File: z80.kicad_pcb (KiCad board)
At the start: 2 copper layers, 104.1 x 111.8 mm, 43 parts, among them P1 CONN_02X20, P2 CONN_01X02, SW1 RESET, U1 Z80CPU, U2 74HC04, U3 74LS138, Y1 7.3728MHz

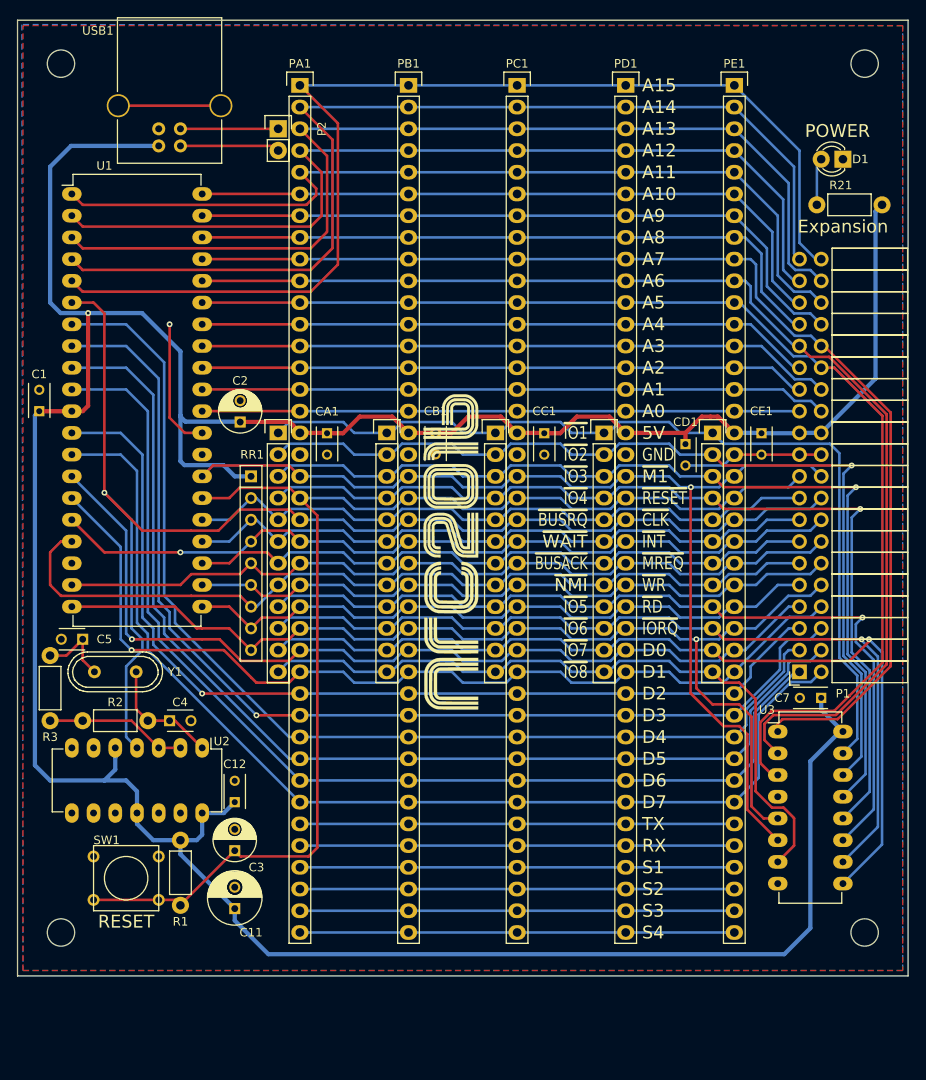
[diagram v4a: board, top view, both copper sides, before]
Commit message: Added new expansion and GAL to layout.
Haven't routed the osc. or the reset.
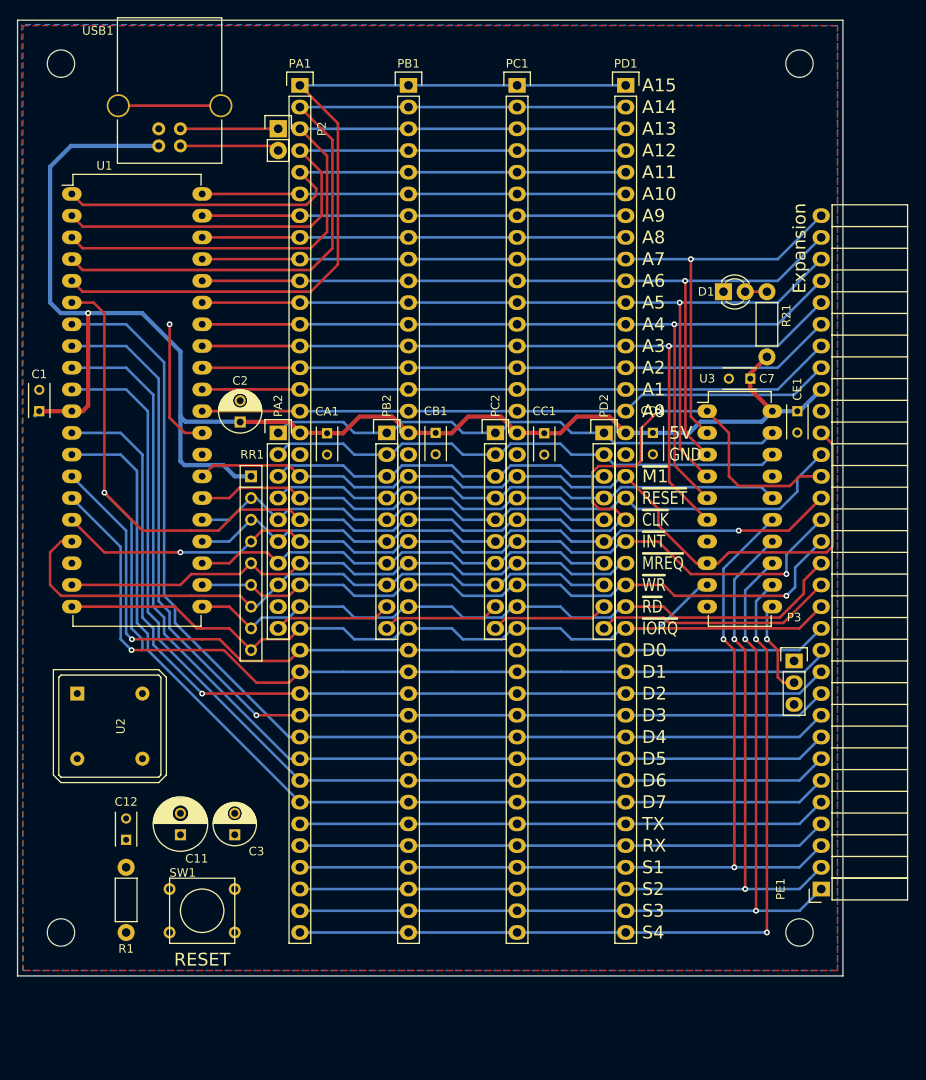
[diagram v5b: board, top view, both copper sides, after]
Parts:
- removed C4, C5: 22pF, Capacitors_ThroughHole:C_Disc_D3_P2.5
- removed G***: LOGO, ncr2016_logo:nrc2016_logo_1200
- removed G***: LOGO, ncr2016_logo:nrc2016_top_logo_1600
- removed P1: CONN_02X20, Socket_Strips:Socket_Strip_Angled_2x20
- removed PE2: CONN_01X12, Socket_Strips:Socket_Strip_Straight_1x12
- removed R2: 1M, Resistors_ThroughHole:Resistor_Horizontal_RM7mm
- removed R3: 1K, Resistors_ThroughHole:Resistor_Horizontal_RM7mm
- removed Y1: 7.3728MHz, Crystals:Crystal_HC49-U_Vertical
- added P3: Jumper, Pin_Headers:Pin_Header_Straight_1x03, F.Cu at (131.4, 105.4)
- PA2, PB2, PC2, PD2: value CONN_01X12 -> CONN_01X10; footprint Socket_Strips:Socket_Strip_Straight_1x12 -> Socket_Strips:Socket_Strip_Straight_1x10
- PE1: value CONN_01X40 -> CONN_01X32; footprint Socket_Strips:Socket_Strip_Straight_1x40 -> Socket_Strips:Socket_Strip_Angled_1x32
- U2: value 74HC04 -> DIP_OSCILLATOR; footprint Housings_DIP:DIP-14_W7.62mm_LongPads -> Oscillators:OSC_DIP8
- U3: value 74LS138 -> ATF16V8CV; footprint Housings_DIP:DIP-16_W7.62mm_LongPads -> Housings_DIP:DIP-20_W7.62mm_LongPads
- moved PE1 94.5 mm to (134.6, 132.1), turned to 90 degrees
- moved U3 38.4 mm to (121.3, 76.2)
- moved C7 38.2 mm to (126.3, 72.4)
- moved R21 22.3 mm to (128.3, 69.8), turned to 90 degrees
- moved D1 20.9 mm to (123.2, 62.2), turned to 0 degrees
- moved C12 13.4 mm to (53.3, 126.3)
- moved U2 11.1 mm to (51.4, 113.0)
- moved C11 10.7 mm to (59.7, 125.7)
- moved SW1 9.67 mm to (62.2, 134.6)
- moved MH2 7.62 mm to (132.1, 35.6)
- moved MH4 7.62 mm to (132.1, 137.2)
- moved R1 7.10 mm to (53.3, 129.5)
- moved CE1 4.92 mm to (131.8, 76.2)
- moved CD1 4.03 mm to (114.9, 78.7)
- moved C3 1.86 mm to (66.0, 125.7)
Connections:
- net /CPU/~BUSACK renamed /~BUSACK
- net /CPU/~BUSRQ renamed /~BUSRQ
- net /CPU/~NMI renamed /~NMI
- C3 pad 1: /CPU/~RESET -> /~RESET
- PA1 pad 1: /CPU/A15 -> /A15
- PA1 pad 10: /CPU/A6 -> /A6
- PA1 pad 11: /CPU/A5 -> /A5
- PA1 pad 12: /CPU/A4 -> /A4
- PA1 pad 13: /CPU/A3 -> /A3
- PA1 pad 14: /CPU/A2 -> /A2
- PA1 pad 15: /CPU/A1 -> /A1
- PA1 pad 16: /CPU/A0 -> /A0
- PA1 pad 19: /CPU/~M1 -> /~M1
- PA1 pad 2: /CPU/A14 -> /A14
- PA1 pad 20: /CPU/~RESET -> /~RESET
- PA1 pad 21: /CPU/~CLK -> /~CLK
- PA1 pad 22: /CPU/~INT -> /~INT
- PA1 pad 23: /CPU/~MREQ -> /~MREQ
- PA1 pad 24: /CPU/~WR -> /~WR
- PA1 pad 25: /CPU/~RD -> /~RD
- PA1 pad 26: /CPU/~IORQ -> /~IORQ
- PA1 pad 27: /CPU/D0 -> /D0
- PA1 pad 28: /CPU/D1 -> /D1
- PA1 pad 29: /CPU/D2 -> /D2
- PA1 pad 3: /CPU/A13 -> /A13
- PA1 pad 30: /CPU/D3 -> /D3
- PA1 pad 31: /CPU/D4 -> /D4
- PA1 pad 32: /CPU/D5 -> /D5
- PA1 pad 33: /CPU/D6 -> /D6
- PA1 pad 34: /CPU/D7 -> /D7
- PA1 pad 35: /Card Slots/PortA/TX -> /Card Slots/TX
- PA1 pad 36: /Card Slots/PortA/RX -> /Card Slots/RX
- PA1 pad 37: /Card Slots/PortA/SPARE1 -> /Card Slots/S1
- PA1 pad 38: /Card Slots/PortA/SPARE2 -> /Card Slots/S2
- PA1 pad 39: /Card Slots/PortA/SPARE3 -> /Card Slots/S3
- PA1 pad 4: /CPU/A12 -> /A12
- PA1 pad 40: /Card Slots/PortA/SPARE4 -> /Card Slots/S4
- PA1 pad 5: /CPU/A11 -> /A11
- PA1 pad 6: /CPU/A10 -> /A10
- PA1 pad 7: /CPU/A9 -> /A9
- PA1 pad 8: /CPU/A8 -> /A8
- PA1 pad 9: /CPU/A7 -> /A7
- PA2 pad 1: /Card Slots/PortA/~IOSEL1 -> /Card Slots/~IOSEL0
- PA2 pad 10: /Card Slots/PortA/~IOSEL6 -> /Card Slots/PortB/IEI
- PA2 pad 2: /Card Slots/PortA/~IOSEL2 -> /Card Slots/~IOSEL1
- PA2 pad 3: /Card Slots/PortA/~IOSEL3 -> /Card Slots/~IOSEL2
- PA2 pad 4: /Card Slots/PortA/~IOSEL4 -> /Card Slots/~IOSEL3
- PA2 pad 6: /CPU/~WAIT -> /~WAIT
- PA2 pad 9: /Card Slots/PortA/~IOSEL5 -> VCC
- PB1 pad 1: /CPU/A15 -> /A15
- PB1 pad 10: /CPU/A6 -> /A6
- PB1 pad 11: /CPU/A5 -> /A5
- PB1 pad 12: /CPU/A4 -> /A4
- PB1 pad 13: /CPU/A3 -> /A3
- PB1 pad 14: /CPU/A2 -> /A2
- PB1 pad 15: /CPU/A1 -> /A1
- PB1 pad 16: /CPU/A0 -> /A0
- PB1 pad 19: /CPU/~M1 -> /~M1
- PB1 pad 2: /CPU/A14 -> /A14
- PB1 pad 20: /CPU/~RESET -> /~RESET
- PB1 pad 21: /CPU/~CLK -> /~CLK
- PB1 pad 22: /CPU/~INT -> /~INT
- PB1 pad 23: /CPU/~MREQ -> /~MREQ
- PB1 pad 24: /CPU/~WR -> /~WR
- PB1 pad 25: /CPU/~RD -> /~RD
- PB1 pad 26: /CPU/~IORQ -> /~IORQ
- PB1 pad 27: /CPU/D0 -> /D0
- PB1 pad 28: /CPU/D1 -> /D1
- PB1 pad 29: /CPU/D2 -> /D2
- PB1 pad 3: /CPU/A13 -> /A13
- PB1 pad 30: /CPU/D3 -> /D3
- PB1 pad 31: /CPU/D4 -> /D4
- PB1 pad 32: /CPU/D5 -> /D5
- PB1 pad 33: /CPU/D6 -> /D6
- PB1 pad 34: /CPU/D7 -> /D7
- PB1 pad 35: /Card Slots/PortA/TX -> /Card Slots/TX
- PB1 pad 36: /Card Slots/PortA/RX -> /Card Slots/RX
- PB1 pad 37: /Card Slots/PortA/SPARE1 -> /Card Slots/S1
- PB1 pad 38: /Card Slots/PortA/SPARE2 -> /Card Slots/S2
- PB1 pad 39: /Card Slots/PortA/SPARE3 -> /Card Slots/S3
- PB1 pad 4: /CPU/A12 -> /A12
- PB1 pad 40: /Card Slots/PortA/SPARE4 -> /Card Slots/S4
- PB1 pad 5: /CPU/A11 -> /A11
- PB1 pad 6: /CPU/A10 -> /A10
- PB1 pad 7: /CPU/A9 -> /A9
- PB1 pad 8: /CPU/A8 -> /A8
- PB1 pad 9: /CPU/A7 -> /A7
- PB2 pad 1: /Card Slots/PortA/~IOSEL1 -> /Card Slots/~IOSEL0
- PB2 pad 10: /Card Slots/PortA/~IOSEL6 -> /Card Slots/PortC/IEI
- PB2 pad 2: /Card Slots/PortA/~IOSEL2 -> /Card Slots/~IOSEL1
- PB2 pad 3: /Card Slots/PortA/~IOSEL3 -> /Card Slots/~IOSEL2
- PB2 pad 4: /Card Slots/PortA/~IOSEL4 -> /Card Slots/~IOSEL3
- PB2 pad 6: /CPU/~WAIT -> /~WAIT
- PB2 pad 9: /Card Slots/PortA/~IOSEL5 -> /Card Slots/PortB/IEI
- PC1 pad 1: /CPU/A15 -> /A15
- PC1 pad 10: /CPU/A6 -> /A6
- PC1 pad 11: /CPU/A5 -> /A5
- PC1 pad 12: /CPU/A4 -> /A4
- PC1 pad 13: /CPU/A3 -> /A3
- PC1 pad 14: /CPU/A2 -> /A2
- PC1 pad 15: /CPU/A1 -> /A1
- PC1 pad 16: /CPU/A0 -> /A0
- PC1 pad 19: /CPU/~M1 -> /~M1
- PC1 pad 2: /CPU/A14 -> /A14
- PC1 pad 20: /CPU/~RESET -> /~RESET
- PC1 pad 21: /CPU/~CLK -> /~CLK
- PC1 pad 22: /CPU/~INT -> /~INT
- PC1 pad 23: /CPU/~MREQ -> /~MREQ
- PC1 pad 24: /CPU/~WR -> /~WR
- PC1 pad 25: /CPU/~RD -> /~RD
- PC1 pad 26: /CPU/~IORQ -> /~IORQ
- PC1 pad 27: /CPU/D0 -> /D0
- PC1 pad 28: /CPU/D1 -> /D1
- PC1 pad 29: /CPU/D2 -> /D2
- PC1 pad 3: /CPU/A13 -> /A13
- PC1 pad 30: /CPU/D3 -> /D3
- PC1 pad 31: /CPU/D4 -> /D4
- PC1 pad 32: /CPU/D5 -> /D5
- PC1 pad 33: /CPU/D6 -> /D6
- PC1 pad 34: /CPU/D7 -> /D7
- PC1 pad 35: /Card Slots/PortA/TX -> /Card Slots/TX
- PC1 pad 36: /Card Slots/PortA/RX -> /Card Slots/RX
- PC1 pad 37: /Card Slots/PortA/SPARE1 -> /Card Slots/S1
- PC1 pad 38: /Card Slots/PortA/SPARE2 -> /Card Slots/S2
- PC1 pad 39: /Card Slots/PortA/SPARE3 -> /Card Slots/S3
- PC1 pad 4: /CPU/A12 -> /A12
- PC1 pad 40: /Card Slots/PortA/SPARE4 -> /Card Slots/S4
- PC1 pad 5: /CPU/A11 -> /A11
- PC1 pad 6: /CPU/A10 -> /A10
- PC1 pad 7: /CPU/A9 -> /A9
- PC1 pad 8: /CPU/A8 -> /A8
- PC1 pad 9: /CPU/A7 -> /A7
- PC2 pad 1: /Card Slots/PortA/~IOSEL1 -> /Card Slots/~IOSEL0
- PC2 pad 10: /Card Slots/PortA/~IOSEL6 -> /Card Slots/PortD/IEI
- PC2 pad 2: /Card Slots/PortA/~IOSEL2 -> /Card Slots/~IOSEL1
- PC2 pad 3: /Card Slots/PortA/~IOSEL3 -> /Card Slots/~IOSEL2
- PC2 pad 4: /Card Slots/PortA/~IOSEL4 -> /Card Slots/~IOSEL3
- PC2 pad 6: /CPU/~WAIT -> /~WAIT
- PC2 pad 9: /Card Slots/PortA/~IOSEL5 -> /Card Slots/PortC/IEI
- PD1 pad 1: /CPU/A15 -> /A15
- PD1 pad 10: /CPU/A6 -> /A6
- PD1 pad 11: /CPU/A5 -> /A5
- PD1 pad 12: /CPU/A4 -> /A4
- PD1 pad 13: /CPU/A3 -> /A3
- PD1 pad 14: /CPU/A2 -> /A2
- PD1 pad 15: /CPU/A1 -> /A1
- PD1 pad 16: /CPU/A0 -> /A0
- PD1 pad 19: /CPU/~M1 -> /~M1
- PD1 pad 2: /CPU/A14 -> /A14
- PD1 pad 20: /CPU/~RESET -> /~RESET
- PD1 pad 21: /CPU/~CLK -> /~CLK
- PD1 pad 22: /CPU/~INT -> /~INT
- PD1 pad 23: /CPU/~MREQ -> /~MREQ
- PD1 pad 24: /CPU/~WR -> /~WR
- PD1 pad 25: /CPU/~RD -> /~RD
- PD1 pad 26: /CPU/~IORQ -> /~IORQ
- PD1 pad 27: /CPU/D0 -> /D0
- PD1 pad 28: /CPU/D1 -> /D1
- PD1 pad 29: /CPU/D2 -> /D2
- PD1 pad 3: /CPU/A13 -> /A13
- PD1 pad 30: /CPU/D3 -> /D3
- PD1 pad 31: /CPU/D4 -> /D4
- PD1 pad 32: /CPU/D5 -> /D5
- PD1 pad 33: /CPU/D6 -> /D6
- PD1 pad 34: /CPU/D7 -> /D7
- PD1 pad 35: /Card Slots/PortA/TX -> /Card Slots/TX
- PD1 pad 36: /Card Slots/PortA/RX -> /Card Slots/RX
- PD1 pad 37: /Card Slots/PortA/SPARE1 -> /Card Slots/S1
- PD1 pad 38: /Card Slots/PortA/SPARE2 -> /Card Slots/S2
- PD1 pad 39: /Card Slots/PortA/SPARE3 -> /Card Slots/S3
- PD1 pad 4: /CPU/A12 -> /A12
- PD1 pad 40: /Card Slots/PortA/SPARE4 -> /Card Slots/S4
- PD1 pad 5: /CPU/A11 -> /A11
- PD1 pad 6: /CPU/A10 -> /A10
- PD1 pad 7: /CPU/A9 -> /A9
- PD1 pad 8: /CPU/A8 -> /A8
- PD1 pad 9: /CPU/A7 -> /A7
- PD2 pad 1: /Card Slots/PortA/~IOSEL1 -> /Card Slots/~IOSEL0
- PD2 pad 10: /Card Slots/PortA/~IOSEL6 -> /Card Slots/Expansion/IEI
- PD2 pad 2: /Card Slots/PortA/~IOSEL2 -> /Card Slots/~IOSEL1
- PD2 pad 3: /Card Slots/PortA/~IOSEL3 -> /Card Slots/~IOSEL2
- PD2 pad 4: /Card Slots/PortA/~IOSEL4 -> /Card Slots/~IOSEL3
- PD2 pad 6: /CPU/~WAIT -> /~WAIT
- PD2 pad 9: /Card Slots/PortA/~IOSEL5 -> /Card Slots/PortD/IEI
- PE1 pad 1: /CPU/A15 -> /Card Slots/S3
- PE1 pad 10: /CPU/A6 -> /D3
- PE1 pad 11: /CPU/A5 -> /D2
- PE1 pad 12: /CPU/A4 -> /D1
- PE1 pad 13: /CPU/A3 -> /D0
- PE1 pad 14: /CPU/A2 -> /~IORQ
- PE1 pad 15: /CPU/A1 -> /Card Slots/Expansion/IEI
- PE1 pad 16: /CPU/A0 -> /~RD
- PE1 pad 17: VCC -> /~WR
- PE1 pad 18: GND -> /~INT
- PE1 pad 19: /CPU/~M1 -> /~WAIT
- PE1 pad 2: /CPU/A14 -> /Card Slots/S2
- PE1 pad 20: /CPU/~RESET -> /~CLK
- PE1 pad 21: /CPU/~CLK -> /~RESET
- PE1 pad 22: /CPU/~INT -> /~M1
- PE1 pad 23: /CPU/~MREQ -> GND
- PE1 pad 24: /CPU/~WR -> VCC
- PE1 pad 25: /CPU/~RD -> /A0
- PE1 pad 26: /CPU/~IORQ -> /A1
- PE1 pad 27: /CPU/D0 -> /A2
- PE1 pad 28: /CPU/D1 -> /A3
- PE1 pad 29: /CPU/D2 -> /A4
- PE1 pad 3: /CPU/A13 -> /Card Slots/S1
- PE1 pad 30: /CPU/D3 -> /A5
- PE1 pad 31: /CPU/D4 -> /A6
- PE1 pad 32: /CPU/D5 -> /A7
- PE1 pad 4: /CPU/A12 -> /Card Slots/RX
- PE1 pad 5: /CPU/A11 -> /Card Slots/TX
- PE1 pad 6: /CPU/A10 -> /D7
- PE1 pad 7: /CPU/A9 -> /D6
- PE1 pad 8: /CPU/A8 -> /D5
- PE1 pad 9: /CPU/A7 -> /D4
- R1 pad 2: /CPU/~RESET -> /~RESET
- RR1 pad 3: /CPU/~WAIT -> /~WAIT
- RR1 pad 4: /CPU/~INT -> /~INT
- RR1 pad 5: /CPU/~MREQ -> /~MREQ
- RR1 pad 6: /CPU/~WR -> /~WR
- RR1 pad 8: /CPU/~RD -> /~RD
- RR1 pad 9: /CPU/~IORQ -> /~IORQ
- SW1 pad 2: /CPU/~RESET -> /~RESET
- U1 pad 1: /CPU/A11 -> /A11
- U1 pad 10: /CPU/D6 -> /D6
- U1 pad 12: /CPU/D2 -> /D2
- U1 pad 13: /CPU/D7 -> /D7
- U1 pad 14: /CPU/D0 -> /D0
- U1 pad 15: /CPU/D1 -> /D1
- U1 pad 16: /CPU/~INT -> /~INT
- U1 pad 19: /CPU/~MREQ -> /~MREQ
- U1 pad 2: /CPU/A12 -> /A12
- U1 pad 20: /CPU/~IORQ -> /~IORQ
- U1 pad 21: /CPU/~RD -> /~RD
- U1 pad 22: /CPU/~WR -> /~WR
- U1 pad 24: /CPU/~WAIT -> /~WAIT
- U1 pad 26: /CPU/~RESET -> /~RESET
- U1 pad 27: /CPU/~M1 -> /~M1
- U1 pad 3: /CPU/A13 -> /A13
- U1 pad 30: /CPU/A0 -> /A0
- U1 pad 31: /CPU/A1 -> /A1
- U1 pad 32: /CPU/A2 -> /A2
- U1 pad 33: /CPU/A3 -> /A3
- U1 pad 34: /CPU/A4 -> /A4
- U1 pad 35: /CPU/A5 -> /A5
- U1 pad 36: /CPU/A6 -> /A6
- U1 pad 37: /CPU/A7 -> /A7
- U1 pad 38: /CPU/A8 -> /A8
- U1 pad 39: /CPU/A9 -> /A9
- U1 pad 4: /CPU/A14 -> /A14
- U1 pad 40: /CPU/A10 -> /A10
- U1 pad 5: /CPU/A15 -> /A15
- U1 pad 6: /CPU/~CLK -> /~CLK
- U1 pad 7: /CPU/D4 -> /D4
- U1 pad 8: /CPU/D3 -> /D3
- U1 pad 9: /CPU/D5 -> /D5
- U2 pad 1: Net-(C4-Pad1) -> (no net)
- U2 pad 4: /CPU/~CLK -> (no net)
- U2 pad 5: VCC -> (no net)
- U2 pad 8: (no net) -> /~CLK
- U3 pad 1: /CPU/A7 -> /~CLK
- U3 pad 10: /Card Slots/PortA/~IOSEL6 -> (no net)
- U3 pad 11: /Card Slots/PortA/~IOSEL5 -> Net-(P3-Pad2)
- U3 pad 12: /Card Slots/PortA/~IOSEL4 -> /Card Slots/S4
- U3 pad 13: /Card Slots/PortA/~IOSEL3 -> /Card Slots/S3
- U3 pad 14: /Card Slots/PortA/~IOSEL2 -> /Card Slots/S2
- U3 pad 15: /Card Slots/PortA/~IOSEL1 -> /Card Slots/S1
- U3 pad 16: VCC -> /Card Slots/~IOSEL3
- U3 pad 2: /CPU/A6 -> /A7
- U3 pad 3: /CPU/A5 -> /A6
- U3 pad 4: GND -> /A5
- U3 pad 5: /CPU/~IORQ -> /A4
- U3 pad 6: /CPU/~M1 -> /A3
- U3 pad 7: /Card Slots/PortA/~IOSEL8 -> (no net)
- U3 pad 8: GND -> /~M1
- U3 pad 9: /Card Slots/PortA/~IOSEL7 -> /~IORQ
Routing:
- net VCC: track 389.7 -> 177.6 mm
- net /~CLK: track 0.00 -> 160.3 mm, vias 0 -> 2
- net /CPU/~CLK: track 150.7 -> 0.00 mm, vias 1 -> 0
- net /CPU/~RESET: track 147.6 -> 0.00 mm
- net /CPU/A5: track 138.5 -> 0.00 mm
- net /CPU/A6: track 138.1 -> 0.00 mm
- net /CPU/A7: track 136.7 -> 0.00 mm
- net /CPU/A15: track 131.5 -> 0.00 mm
- net /CPU/D5: track 130.3 -> 0.00 mm
- net /CPU/D4: track 128.6 -> 0.00 mm
- net /CPU/D3: track 127.6 -> 0.00 mm, vias 1 -> 0
- net /CPU/D6: track 127.4 -> 0.00 mm
- net /CPU/D7: track 126.7 -> 0.00 mm
- net /D4: track 0.00 -> 125.8 mm
- net /CPU/~M1: track 125.3 -> 0.00 mm, vias 1 -> 0
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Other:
- board size 104.1 x 111.8 mm -> 96.5 x 111.8 mm
- board text removed: "POWER"
- board text removed: "~BUSACK"
- board text removed: "~BUSRQ"
- board text removed: "~IO1"
- board text removed: "~IO2"
- board text removed: "~IO3"
- board text removed: "~IO4"
- board text removed: "~IO5"
- board text removed: "~IO6"
- board text removed: "~IO7"
- board text removed: "~IO8"
- board text removed: "~NMI"
- board text removed: "~WAIT"

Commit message: Updated layout to clean up the power rails
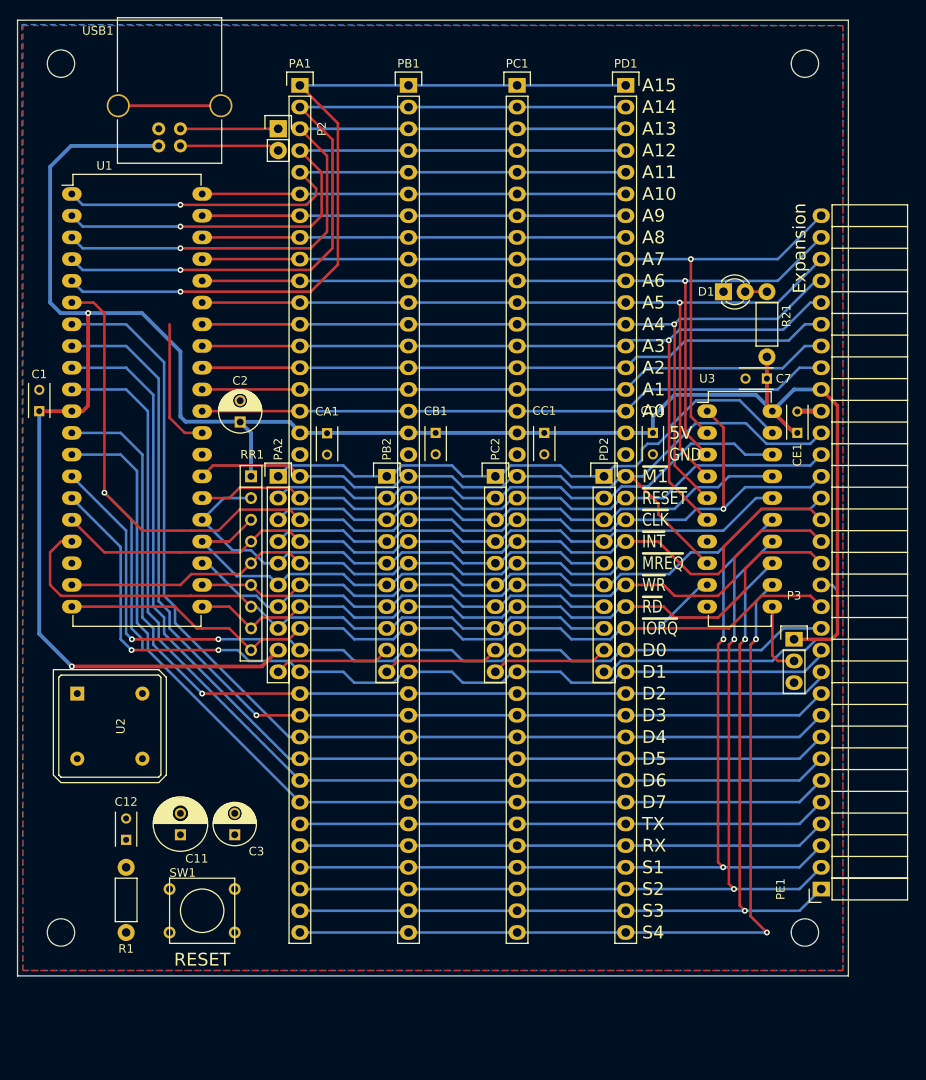
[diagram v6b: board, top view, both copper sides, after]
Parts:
- moved PA2 5.08 mm to (71.1, 83.8)
- moved PB2 5.08 mm to (83.8, 83.8)
- moved PC2 5.08 mm to (96.5, 83.8)
- moved PD2 5.08 mm to (109.2, 83.8)
- moved CE1 2.54 mm to (131.8, 78.7), turned to 90 degrees
- moved P3 2.54 mm to (131.4, 102.9)
- moved C7 1.95 mm to (128.3, 72.4)
- moved MH2 0.63 mm to (132.7, 35.6)
- moved MH4 0.63 mm to (132.7, 137.2)
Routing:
- net VCC: track 177.6 -> 260.3 mm, vias 1 -> 2
- net /Card Slots/~IOSEL2: track 41.3 -> 63.0 mm
- net /~CLK: track 160.3 -> 150.2 mm
- net /~WAIT: track 79.8 -> 88.6 mm, vias 1 -> 0
- net /Card Slots/Expansion/IEI: track 28.0 -> 36.4 mm
- net /~BUSRQ: track 52.8 -> 59.0 mm
- net GND: track 15.5 -> 21.2 mm, vias 1 -> 0
- net /Card Slots/~IOSEL0: track 61.9 -> 67.3 mm
- net /~M1: track 97.9 -> 95.2 mm
- net Net-(P3-Pad2): track 11.2 -> 8.52 mm, vias 1 -> 0
- net /Card Slots/~IOSEL1: track 61.9 -> 64.1 mm
- net /D1: track 104.8 -> 106.9 mm, vias 1 -> 2
- net /D0: track 105.2 -> 107.3 mm, vias 1 -> 2
- net /~RESET: track 80.6 -> 78.6 mm
- net /~RD: track 81.7 -> 83.3 mm
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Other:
- board size 96.5 x 111.8 mm -> 97.2 x 111.8 mm
- net class power: trace_width 0.5 -> 0.45

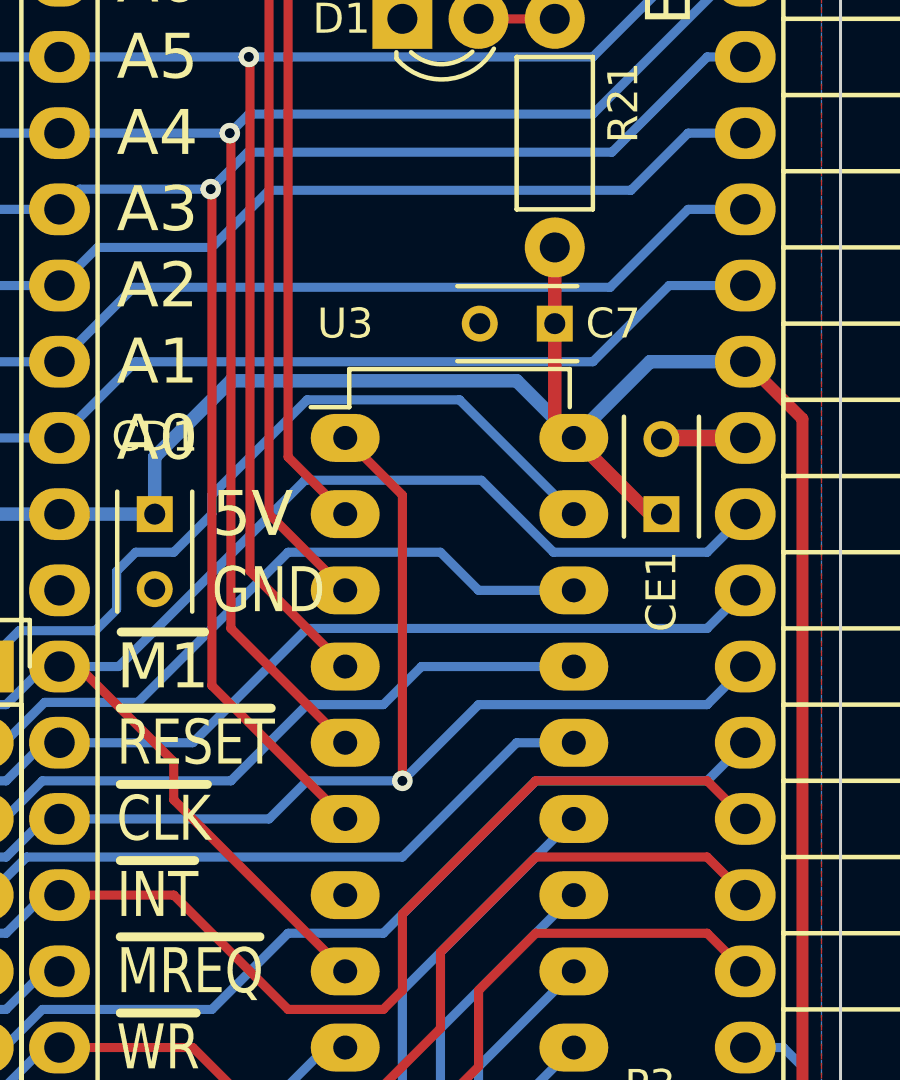
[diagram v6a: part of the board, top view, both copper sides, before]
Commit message: Noticed missing pin I6 on GAL, added A2 input
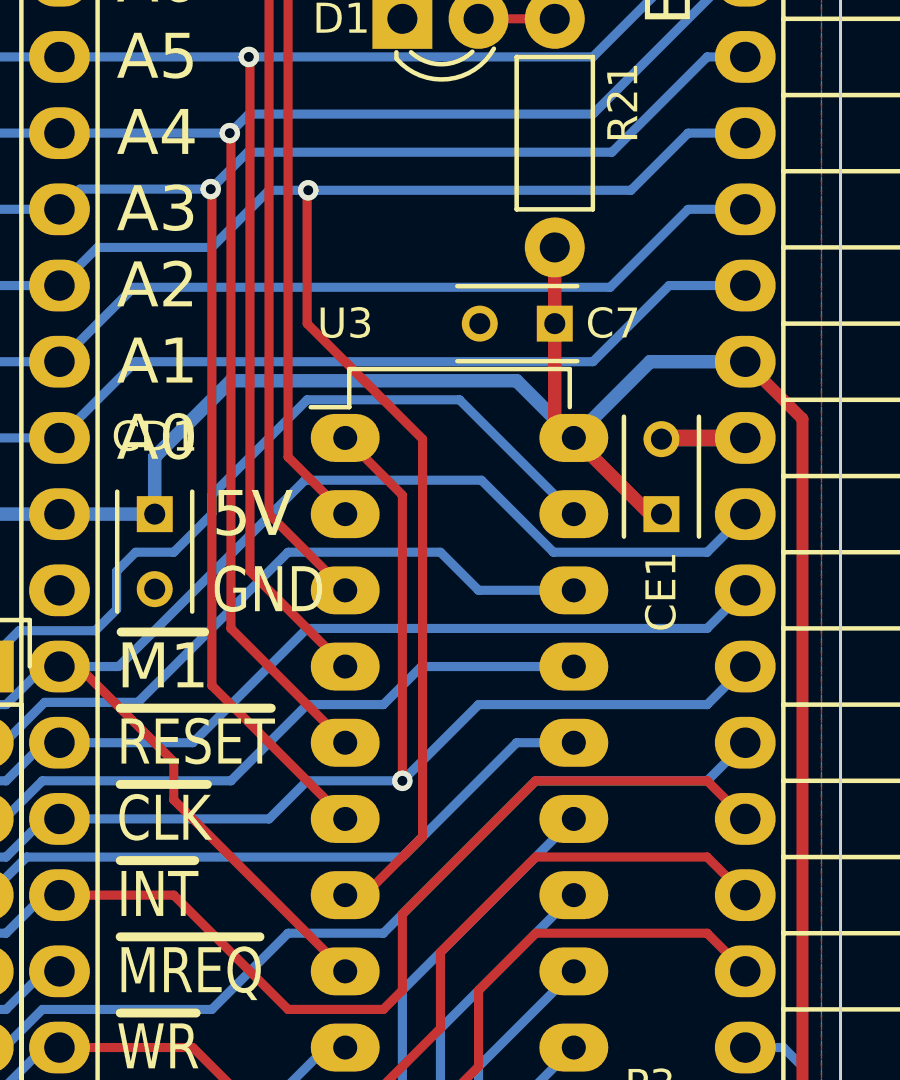
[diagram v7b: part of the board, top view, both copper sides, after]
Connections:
- U3 pad 7: (no net) -> /A2
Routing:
- net /A2: track 74.5 -> 101.1 mm, vias 0 -> 1
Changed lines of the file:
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@@
 (kicad_pcb (version 4) (host pcbnew 4.0.2-stable)
   (general
-    (links 284)
+    (links 285)
     (no_connects 10)
     (area 40.589999 30.429999 137.845001 142.290001)
     (thickness 1.6002)
     (drawings 46)
-    (tracks 824)
+    (tracks 833)
     (zones 0)
     (modules 35)
@@
     (pad 6 thru_hole oval (at 0 12.7) (size 2.3 1.6) (drill 0.8) (layers *.Cu *.Mask F.SilkS)
       (net 21 /A3))
-    (pad 7 thru_hole oval (at 0 15.24) (size 2.3 1.6) (drill 0.8) (layers *.Cu *.Mask F.SilkS))
+    (pad 7 thru_hole oval (at 0 15.24) (size 2.3 1.6) (drill 0.8) (layers *.Cu *.Mask F.SilkS)
+      (net 22 /A2))
     (pad 8 thru_hole oval (at 0 17.78) (size 2.3 1.6) (drill 0.8) (layers *.Cu *.Mask F.SilkS)
       (net 25 /~M1))
@@
   (segment (start 86.36 68.58) (end 99.06 68.58) (width 0.3048) (layer Bottom) (net 21))
   (segment (start 99.06 68.58) (end 111.76 68.58) (width 0.3048) (layer Bottom) (net 21))
+  (segment (start 120.0531 67.945) (end 120.015 67.9831) (width 0.3048) (layer Top) (net 22))
+  (segment (start 120.015 67.9831) (end 120.015 72.39) (width 0.3048) (layer Top) (net 22))
+  (segment (start 120.015 72.39) (end 123.863101 76.238101) (width 0.3048) (layer Top) (net 22))
+  (segment (start 123.863101 76.238101) (end 123.863101 89.496899) (width 0.3048) (layer Top) (net 22))
+  (segment (start 123.863101 89.496899) (end 121.92 91.44) (width 0.3048) (layer Top) (net 22))
+  (segment (start 121.92 91.44) (end 121.285 91.44) (width 0.3048) (layer Top) (net 22))
+  (segment (start 120.015 67.945) (end 130.81 67.945) (width 0.3048) (layer Bottom) (net 22))
+  (segment (start 120.015 67.945) (end 120.0531 67.945) (width 0.3048) (layer Bottom) (net 22))
+  (segment (start 118.745 67.945) (end 120.015 67.945) (width 0.3048) (layer Bottom) (net 22))
+  (via (at 120.0531 67.945) (size 0.6858) (drill 0.3302) (layers Top Bottom) (net 22))
   (segment (start 111.76 71.12) (end 113.03 69.85) (width 0.3048) (layer Bottom) (net 22))
   (segment (start 113.03 69.85) (end 116.84 69.85) (width 0.3048) (layer Bottom) (net 22))
   (segment (start 116.84 69.85) (end 118.745 67.945) (width 0.3048) (layer Bottom) (net 22))
-  (segment (start 118.745 67.945) (end 130.81 67.945) (width 0.3048) (layer Bottom) (net 22))
   (segment (start 130.81 67.945) (end 132.715 66.04) (width 0.3048) (layer Bottom) (net 22))
   (segment (start 132.715 66.04) (end 134.62 66.04) (width 0.3048) (layer Bottom) (net 22))

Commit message: More OCD PCB fiddling, cleaning up traces etc
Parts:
- moved CA1 1.27 mm to (76.8, 77.5)
- moved CC1 1.27 mm to (102.2, 77.5)
- moved CB1 1.23 mm to (89.5, 77.5)
- moved CD1 1.23 mm to (114.9, 77.5)
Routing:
- net VCC: track 260.3 -> 265.1 mm
- net /Card Slots/S4: track 97.1 -> 92.5 mm
- net /Card Slots/~IOSEL3: track 63.0 -> 67.0 mm
- net /~WAIT: track 88.6 -> 91.2 mm
- net /~CLK: track 150.2 -> 152.8 mm
- net /Card Slots/S3: track 104.5 -> 102.0 mm
- net /Card Slots/~IOSEL0: track 67.3 -> 64.8 mm
- net /Card Slots/S2: track 105.0 -> 103.2 mm
- net /A2: track 101.1 -> 102.6 mm
- net /Card Slots/~IOSEL1: track 64.1 -> 63.0 mm
- net /~M1: track 95.2 -> 94.3 mm
- net /~NMI: track 76.9 -> 77.7 mm
- net /~BUSRQ: track 59.0 -> 59.8 mm
- net /~BUSACK: track 52.3 -> 53.0 mm
- net /A5: track 96.1 -> 96.7 mm
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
